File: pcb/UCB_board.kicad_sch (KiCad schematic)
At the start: 29 parts

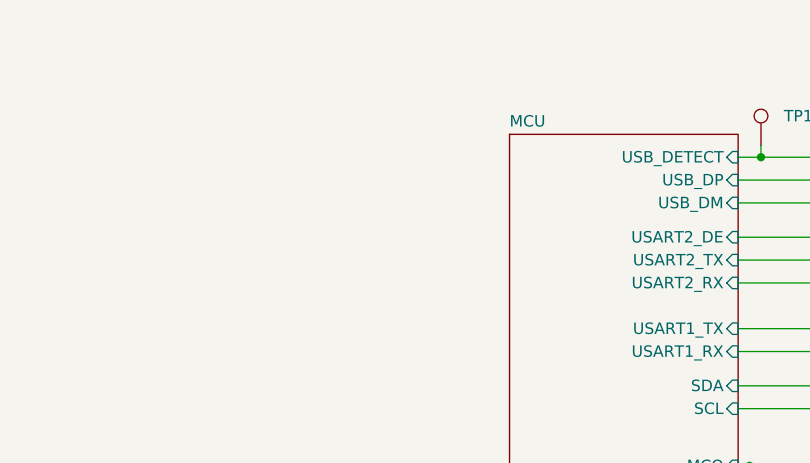
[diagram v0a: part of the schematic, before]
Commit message: Add UniConnector for io expansion (2.0mm pinheader)
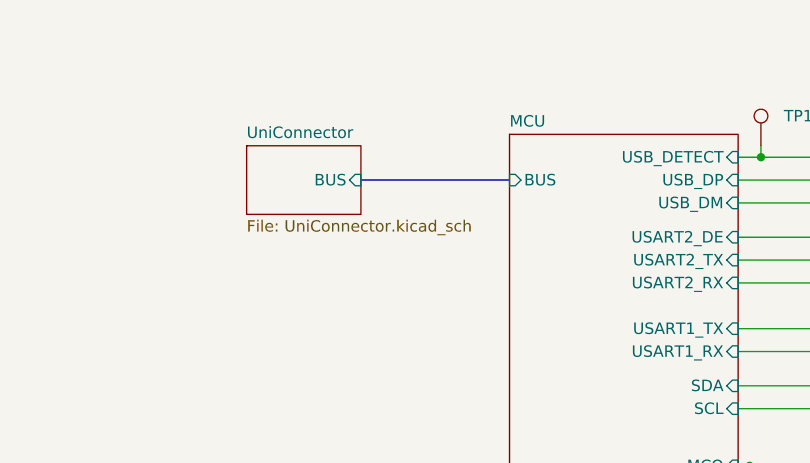
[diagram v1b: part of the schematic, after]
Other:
- added sheet UniConnector (UniConnector.kicad_sch)
- sheet MCU ports: added BUS; removed none
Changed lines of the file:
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@@
+		)
+	)
+	(bus
+		(pts
+			(xy 69.85 71.12) (xy 86.36 71.12)
+		)
+		(stroke
+			(width 0)
+			(type default)
 		)
 	)
@@
 	)
 	(sheet
-		(at 86.36 66.04)
-		(size 25.4 55.88)
+		(at 57.15 67.31)
+		(size 12.7 7.62)
 		(exclude_from_sim no)
 		(in_bom yes)
@@
 			(color 0 0 0 0.0000)
 		)
+		(property "Sheetname" "UniConnector"
+			(at 57.15 66.5984 0)
+			(effects
+				(font
+					(size 1.27 1.27)
+				)
+				(justify left bottom)
+			)
+		)
+		(property "Sheetfile" "UniConnector.kicad_sch"
+			(at 57.15 75.5146 0)
+			(effects
+				(font
+					(size 1.27 1.27)
+				)
+				(justify left top)
+			)
+		)
+		(pin "BUS" input
+			(at 69.85 71.12 0)
+			(effects
+				(font
+					(size 1.27 1.27)
+				)
+				(justify right)
+			)
+		)
+		(instances
+			(project "UCB_board"
+				(path "/0c4edb77-9bdf-4103-be66-c5eb9940b163"
+					(page "6")
+				)
+			)
+		)
+	)
+	(sheet
+		(at 86.36 66.04)
+		(size 25.4 55.88)
+		(exclude_from_sim no)
+		(in_bom yes)
+		(on_board yes)
+		(dnp no)
+		(fields_autoplaced yes)
+		(stroke
+			(width 0.1524)
+			(type solid)
+		)
+		(fill
+			(color 0 0 0 0.0000)
+		)
 		(property "Sheetname" "MCU"
 			(at 86.36 65.3284 0)
@@
 			)
 		)
+		(pin "BUS" input
+			(at 86.36 71.12 180)
+			(effects
+				(font
+					(size 1.27 1.27)
+				)
+				(justify left)
+			)
+		)

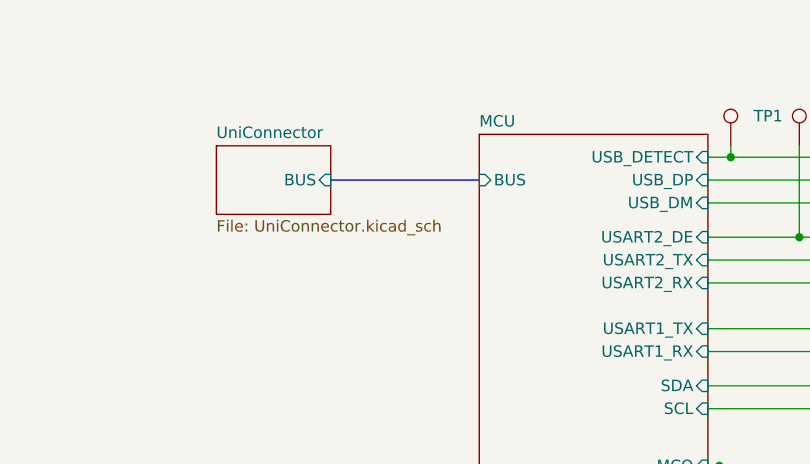
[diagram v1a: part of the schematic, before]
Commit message: UniConnector new traces
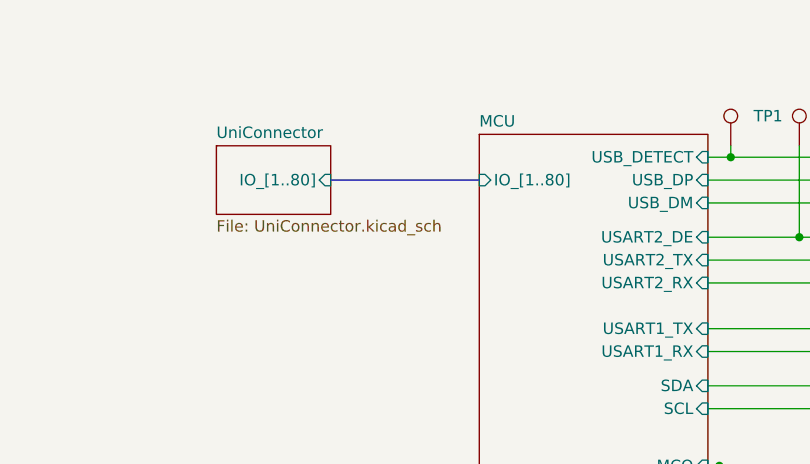
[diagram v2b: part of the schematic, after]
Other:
- sheet MCU ports: added IO_[1..80]; removed BUS
- sheet UniConnector ports: added IO_[1..80]; removed BUS
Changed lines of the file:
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@@
 			)
 		)
-		(pin "BUS" input
+		(pin "IO_[1..80]" input
 			(at 69.85 71.12 0)
 			(effects
@@
 			)
 		)
-		(pin "BUS" input
+		(pin "IO_[1..80]" input
 			(at 86.36 71.12 180)
 			(effects

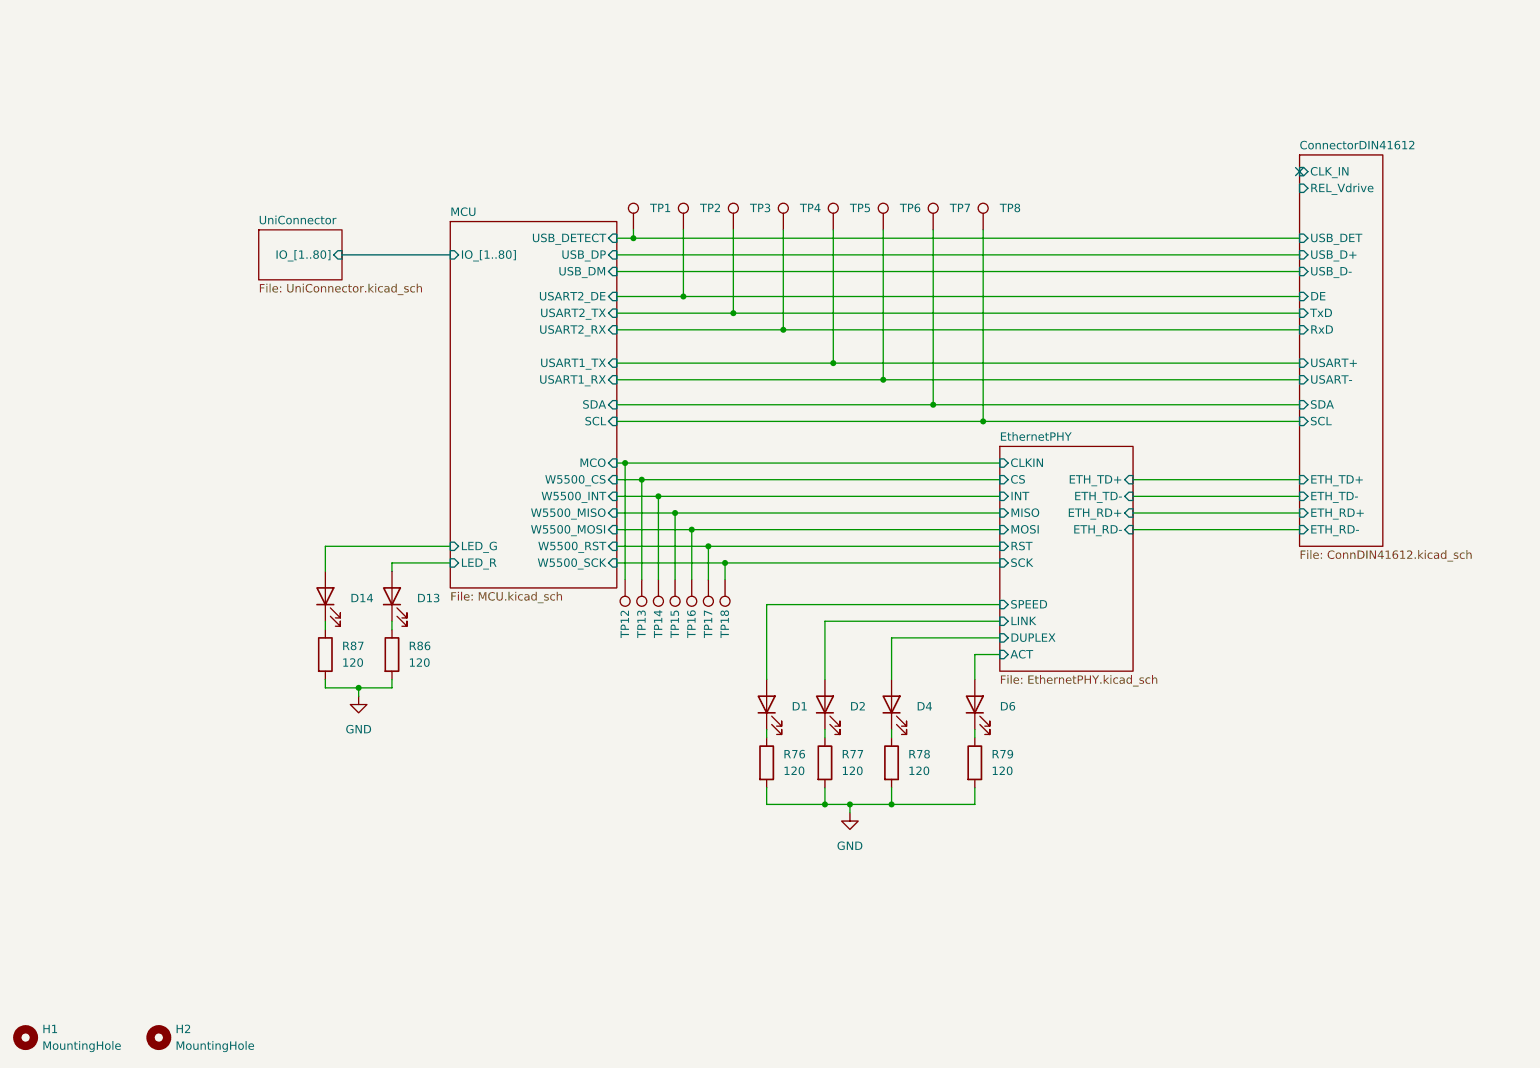
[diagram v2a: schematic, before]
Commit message: Added SI5351C
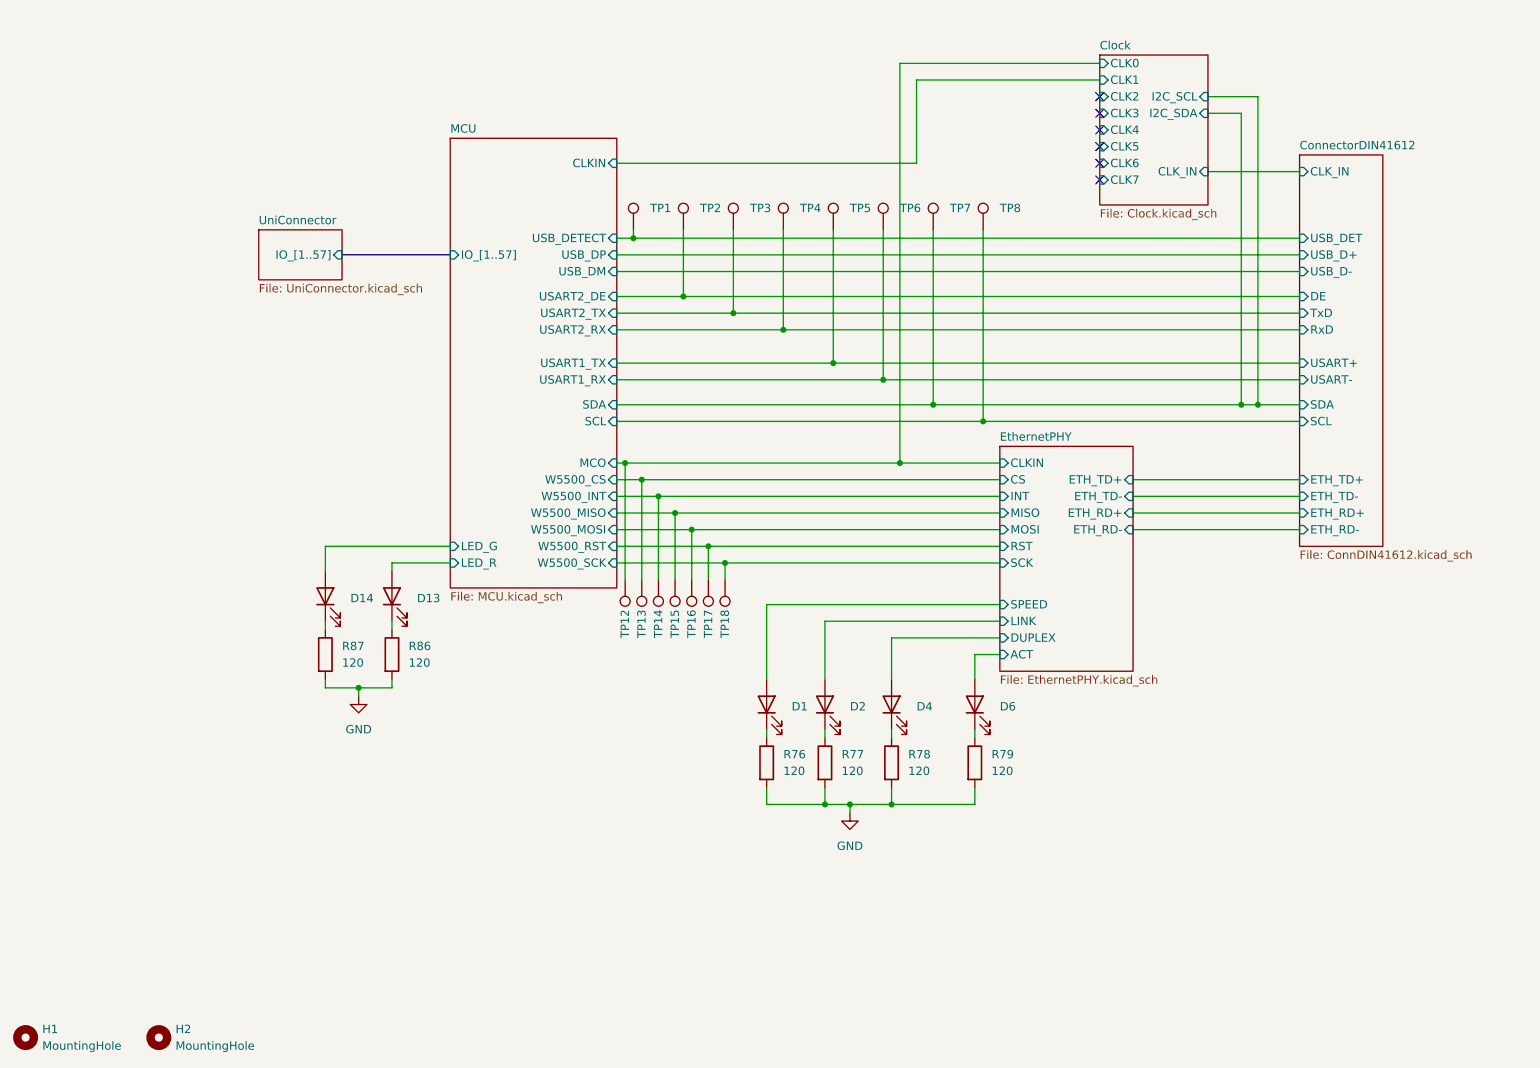
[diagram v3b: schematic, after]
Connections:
- net ConnectorDIN41612/SDA renamed Clock/I2C_SCL
- net EthernetPHY/CLKIN renamed Clock/CLK0
- no-connect marks 1 -> 6
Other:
- added sheet Clock (Clock.kicad_sch)
- sheet ConnectorDIN41612 ports: added none; removed REL_Vdrive
- sheet MCU ports: added CLKIN, IO_[1..57]; removed IO_[1..80]
- sheet UniConnector ports: added IO_[1..57]; removed IO_[1..80]

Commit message: Clock rounting
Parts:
- added R23, R24, R25, R26: 0R, Resistor_SMD:R_0402_1005Metric_Pad0.72x0.64mm_HandSolder, symbol Device:R
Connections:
- net Clock/CLK0: now also R23.2; no longer TP12.1
- net Clock/CLK1: now also R24.2
- net Clock/CLK2: now also R25.2
- net Clock/CLK3: now also R26.2
- new net EthernetPHY/CLKIN: R23.1, TP12.1
- new net MCU/CLKIN: R24.1
- new net UniConnector/CLK_IN1: R25.1
- new net UniConnector/CLK_IN2: R26.1
- no-connect marks 6 -> 4
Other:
- sheet UniConnector ports: added CLK_IN1, CLK_IN2; removed none

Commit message: New routing
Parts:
- removed H1, H2: MountingHole, MountingHole:MountingHole_2.7mm_M2.5, symbol Mechanical:MountingHole
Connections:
- net ConnectorDIN41612/SCL is gone; now on net Clock/I2C_SCL: TP8.1
- net Clock/I2C_SCL: no longer TP7.1
- new net Clock/I2C_SDA: TP7.1
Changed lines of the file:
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@@
-	)
-	(junction
-		(at 209.55 93.98)
-		(diameter 0)
-		(color 0 0 0 0)
 	)
 	(junction
@@
 	)
 	(junction
+		(at 209.55 96.52)
+		(diameter 0)
+		(color 0 0 0 0)
+	)
+	(junction
 		(at 123.19 113.03)
 		(diameter 0)
@@
 	(wire
 		(pts
-			(xy 209.55 46.99) (xy 209.55 93.98)
-		)
-		(stroke
-			(width 0)
-			(type default)
-		)
-	)
-	(wire
-		(pts
 			(xy 111.76 57.15) (xy 157.48 57.15)
 		)
@@
 	(wire
 		(pts
-			(xy 167.64 96.52) (xy 215.9 96.52)
+			(xy 167.64 96.52) (xy 209.55 96.52)
 		)
 		(stroke
@@
 	(wire
 		(pts
-			(xy 207.01 93.98) (xy 209.55 93.98)
+			(xy 209.55 46.99) (xy 209.55 96.52)
 		)
 		(stroke
@@
 	(wire
 		(pts
+			(xy 209.55 96.52) (xy 215.9 96.52)
+		)
+		(stroke
+			(width 0)
+			(type default)
+		)
+	)
+	(wire
+		(pts
 			(xy 111.76 107.95) (xy 118.11 107.95)
 		)
@@
 	(wire
 		(pts
-			(xy 209.55 93.98) (xy 215.9 93.98)
+			(xy 207.01 93.98) (xy 215.9 93.98)
 		)
 		(stroke
@@
 	)
 	(symbol
-		(lib_id "Mechanical:MountingHole")
-		(at 21.59 190.5 0)
-		(unit 1)
-		(exclude_from_sim no)
-		(in_bom no)
-		(on_board yes)
-		(dnp no)
-		(fields_autoplaced yes)
-		(property "Reference" "H1"
-			(at 24.13 189.2299 0)
-			(effects
-				(font
-					(size 1.27 1.27)
-				)
-				(justify left)
-			)
-		)
-		(property "Value" "MountingHole"
-			(at 24.13 191.7699 0)
-			(effects
-				(font
-					(size 1.27 1.27)
-				)
-				(justify left)
-			)
-		)
-		(property "Footprint" "MountingHole:MountingHole_2.7mm_M2.5"
-			(at 21.59 190.5 0)
-			(effects
-				(font
-					(size 1.27 1.27)
-				)
-				(hide yes)
-			)
-		)
-		(property "Datasheet" "~"
-			(at 21.59 190.5 0)
-			(effects
-				(font
-					(size 1.27 1.27)
-				)
-				(hide yes)
-			)
-		)
-		(property "Description" "Mounting Hole without connection"
-			(at 21.59 190.5 0)
-			(effects
-				(font
-					(size 1.27 1.27)
-				)
-				(hide yes)
-			)
-		)
-		(instances
-			(project ""
-				(path "/0c4edb77-9bdf-4103-be66-c5eb9940b163"
-					(reference "H1")
-					(unit 1)
-				)
-			)
-		)
-	)
-	(symbol
 		(lib_id "Connector:TestPoint")
 		(at 129.54 67.31 0)
@@
 					(unit 1)
 				)
-			)
-		)
-	)
-	(symbol
-		(lib_id "Mechanical:MountingHole")
-		(at 41.91 190.5 0)
-		(unit 1)
-		(exclude_from_sim no)
-		(in_bom no)
-		(on_board yes)
-		(dnp no)
-		(fields_autoplaced yes)
-		(property "Reference" "H2"
-			(at 44.45 189.2299 0)
-			(effects
-				(font
-					(size 1.27 1.27)
-				)
-				(justify left)
-			)
-		)
-		(property "Value" "MountingHole"
-			(at 44.45 191.7699 0)
-			(effects
-				(font
-					(size 1.27 1.27)
-				)
-				(justify left)
-			)
-		)
-		(property "Footprint" "MountingHole:MountingHole_2.7mm_M2.5"
-			(at 41.91 190.5 0)
-			(effects
-				(font
-					(size 1.27 1.27)
-				)
-				(hide yes)
-			)
-		)
-		(property "Datasheet" "~"
-			(at 41.91 190.5 0)
-			(effects
-				(font
-					(size 1.27 1.27)
-				)
-				(hide yes)
-			)
-		)
-		(property "Description" "Mounting Hole without connection"
-			(at 41.91 190.5 0)
-			(effects
-				(font
-					(size 1.27 1.27)
-				)
-				(hide yes)
-			)
-		)
-		(instances
-			(project "100x100_eurocard_testboard"
-				(path "/0c4edb77-9bdf-4103-be66-c5eb9940b163"
-					(reference "H2")
-					(unit 1)
-				)

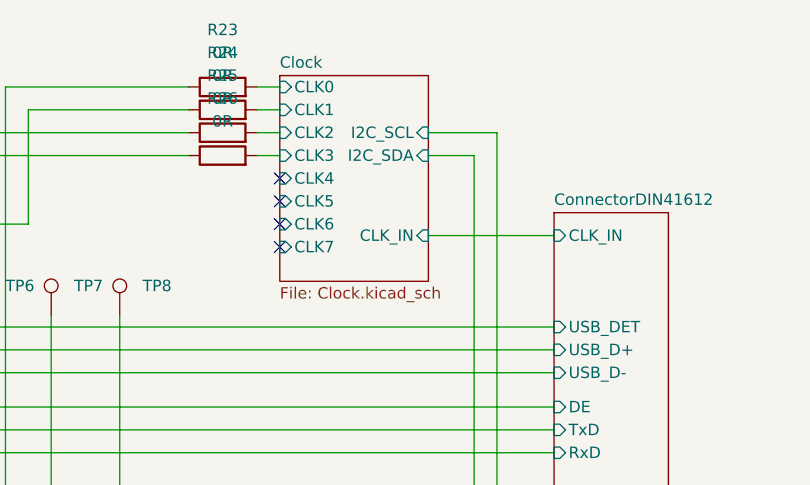
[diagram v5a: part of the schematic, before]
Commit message: Added vias and cleaned pcb. Board finished
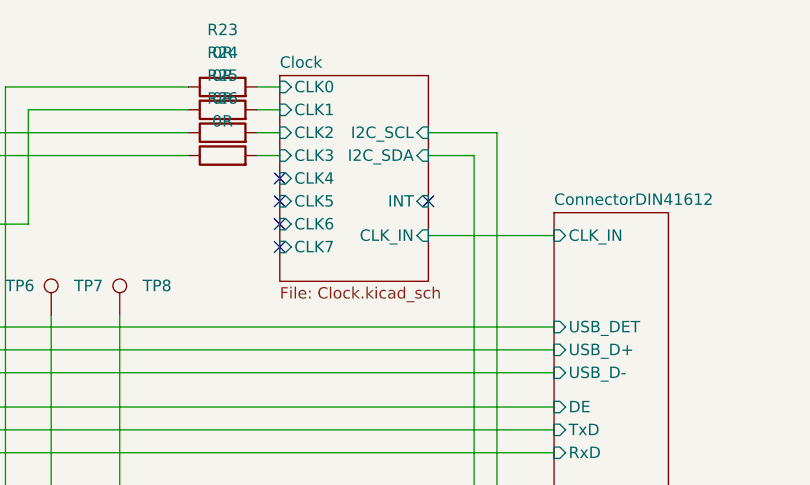
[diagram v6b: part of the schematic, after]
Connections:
- no-connect marks 4 -> 5
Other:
- sheet Clock ports: added INT; removed none
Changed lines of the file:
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@@
 	)
 	(no_connect
+		(at 201.93 54.61)
+	)
+	(no_connect
 		(at 185.42 59.69)
 	)
@@
 			(effects
 				(font
+					(size 1.27 1.27)
+				)
+				(justify right)
+			)
+		)
+		(pin "INT" input
+			(at 201.93 54.61 0)
+			(effects
+				(font

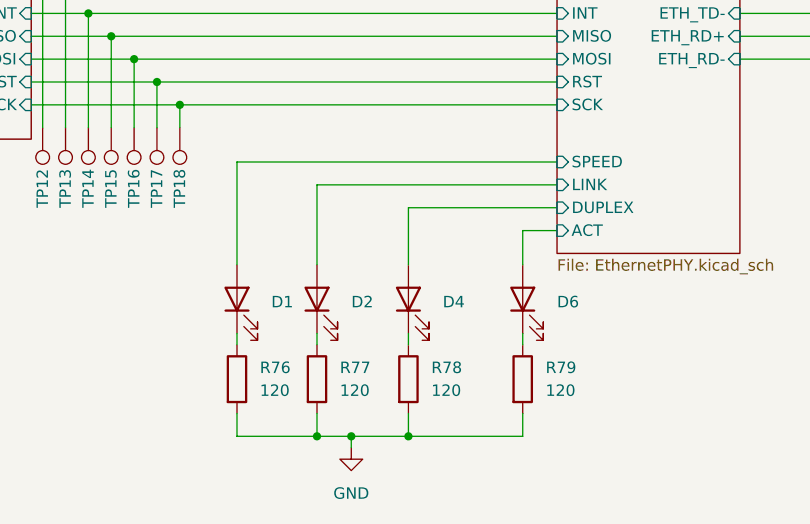
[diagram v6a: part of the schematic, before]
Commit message: Corected mistakes found on RDE_board
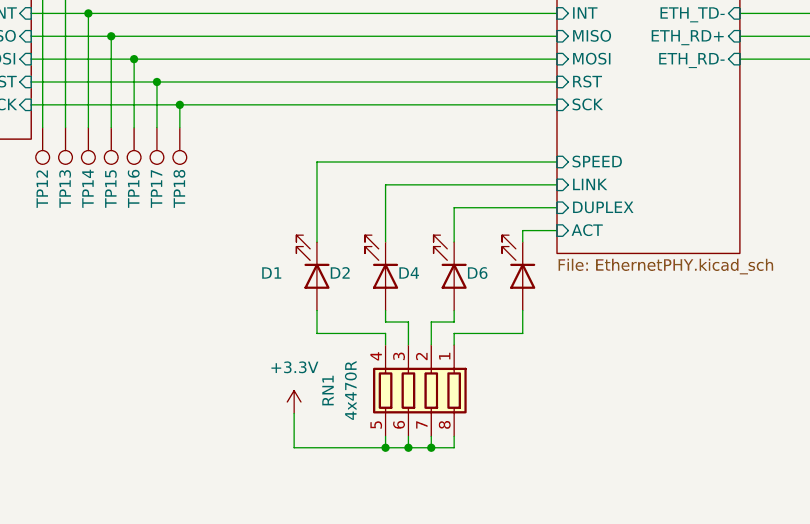
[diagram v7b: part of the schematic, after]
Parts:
- removed R76, R77, R78, R79: 120, Resistor_SMD:R_0603_1608Metric_Pad0.98x0.95mm_HandSolder, symbol Device:R
- added RN1: 4x470R, Resistor_SMD:R_Array_Convex_4x0603, symbol Device:R_Pack04
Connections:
- net EthernetPHY/ACT: now also D6.1 (K); no longer D6.2 (A)
- net EthernetPHY/DUPLEX: now also D4.1 (K); no longer D4.2 (A)
- net EthernetPHY/LINK: now also D2.1 (K); no longer D2.2 (A)
- net EthernetPHY/SPEED: now also D1.1 (K); no longer D1.2 (A)
- new net: D2.2 (A), RN1.3 (R3.1)
- new net: D6.2 (A), RN1.1 (R1.1)
- new net: D4.2 (A), RN1.2 (R2.1)
- new net: D1.2 (A), RN1.4 (R4.1)
- new net +3.3V: RN1.5 (R4.2), RN1.6 (R3.2), RN1.7 (R2.2), RN1.8 (R1.2)
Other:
- moved on the sheet: D1, D2, D4, D6
